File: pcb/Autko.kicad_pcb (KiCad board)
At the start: 2 copper layers, 140 x 155 mm, 124 parts, among them J1 PDI, M1 LEFT, M2 RIGHT, Q1 Si4368DY, Q2 BC817, SW1 POWER, SW2 START, SW3 STOP, U1 LTC3872, U10 CNY70, U11 TB6612FNG, U12 74HC14, U13 RN4678, U2 TLV1117-33, U3 ATxmega16A4U-A, U4 CNY70, U5 CNY70, U6 CNY70, U7 CNY70, U8 CNY70, U9 CNY70, Y1 8MHz

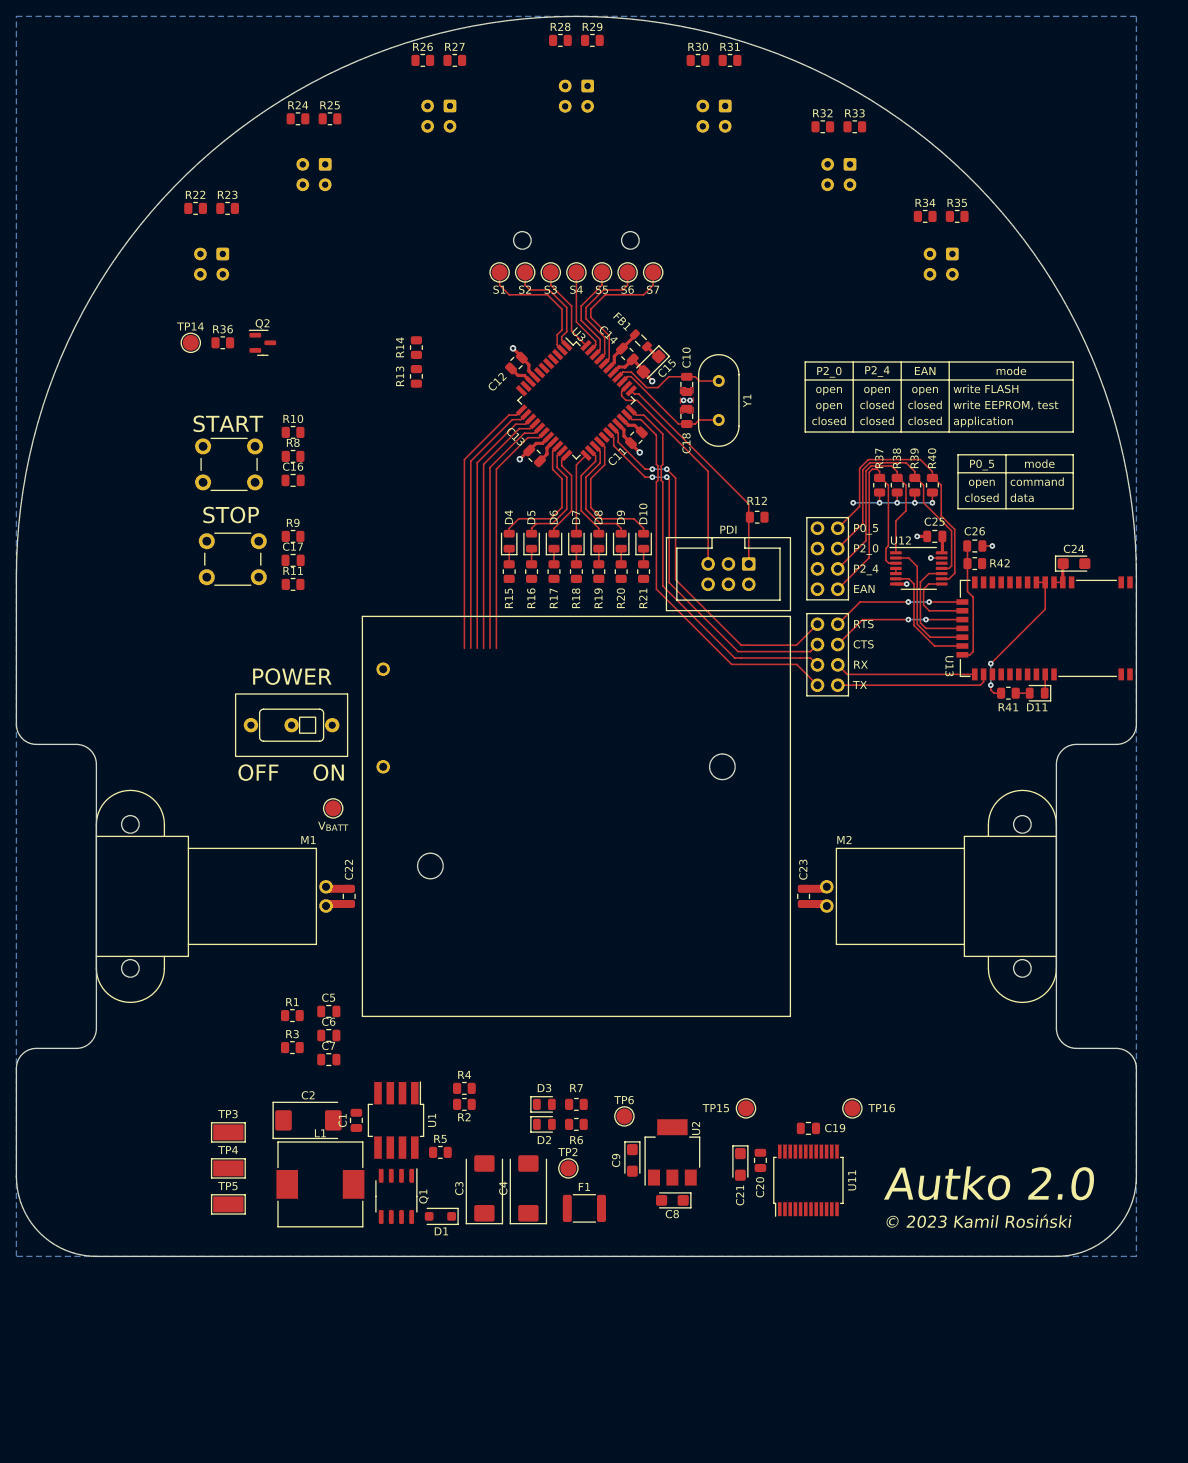
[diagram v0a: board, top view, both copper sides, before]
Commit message: [pcb] Line sensors routed
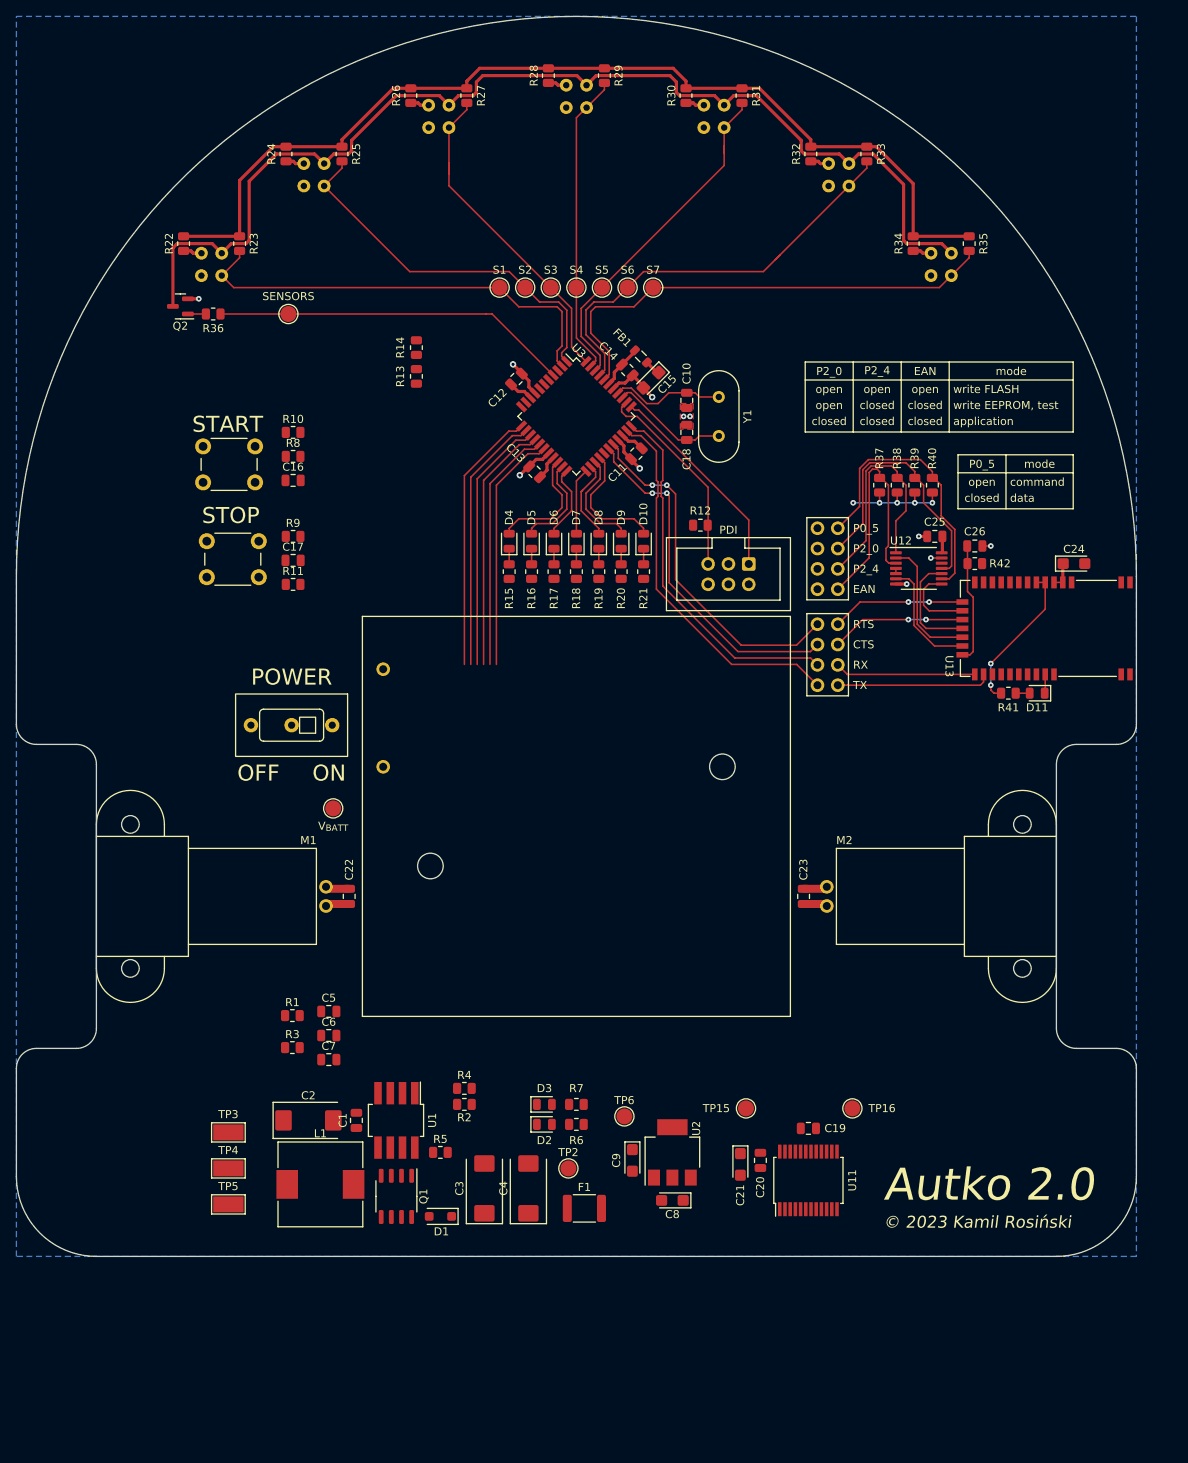
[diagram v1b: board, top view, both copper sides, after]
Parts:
- removed REF**: Pololu_ball_caster, Autko:Pololu_ball_caster
- U10, U4, U5, U6, U7, U8, U9: footprint OptoDevice:Vishay_CNY70 -> Autko:Vishay_CNY70
- moved TP14 12.7 mm to (63.5, 67.7)
- moved Q2 11.3 mm to (50.0, 66.8), turned to 180 degrees
- moved R12 7.17 mm to (115.0, 94.1), turned to 0 degrees
- moved R24 4.65 mm to (63.2, 47.7), turned to -90 degrees
- moved R25 4.65 mm to (70.2, 47.7), turned to -90 degrees
- moved R22 4.65 mm to (50.4, 58.9), turned to -90 degrees
- moved R23 4.65 mm to (57.4, 58.9), turned to -90 degrees
- moved R26 4.65 mm to (78.8, 40.4), turned to -90 degrees
- moved R27 4.65 mm to (85.8, 40.4), turned to -90 degrees
- moved R28 4.65 mm to (96.0, 37.9), turned to -90 degrees
- moved R29 4.65 mm to (103.0, 37.9), turned to -90 degrees
- moved R30 4.65 mm to (113.2, 40.4), turned to -90 degrees
- moved R31 4.65 mm to (120.2, 40.4), turned to -90 degrees
- moved R36 3.79 mm to (54.1, 67.7), turned to 180 degrees
- moved R32 3.72 mm to (128.8, 47.7), turned to -90 degrees
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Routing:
- net Net-(Q2-C): track 0.00 -> 140.2 mm
- net +3.3V: track 32.0 -> 157.6 mm
- net /Line sensors/IR_LEDS_ON: track 0.00 -> 44.8 mm
- net /Line sensors/SENSOR7: track 18.7 -> 60.7 mm
- net /Line sensors/SENSOR1: track 16.3 -> 55.7 mm
- net /Line sensors/SENSOR6: track 15.6 -> 53.5 mm
- net /Line sensors/SENSOR2: track 13.2 -> 47.7 mm
- net /Line sensors/SENSOR5: track 12.6 -> 44.0 mm
- net /Line sensors/SENSOR3: track 11.0 -> 41.7 mm
- net /Line sensors/SENSOR4: track 11.2 -> 38.3 mm
- net Net-(U10-A): track 0.00 -> 2.35 mm
- net Net-(U6-A): track 0.00 -> 2.35 mm
- net Net-(U4-A): track 0.00 -> 2.35 mm
- net Net-(U8-A): track 0.00 -> 2.35 mm
- net Net-(U7-A): track 0.00 -> 2.35 mm
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
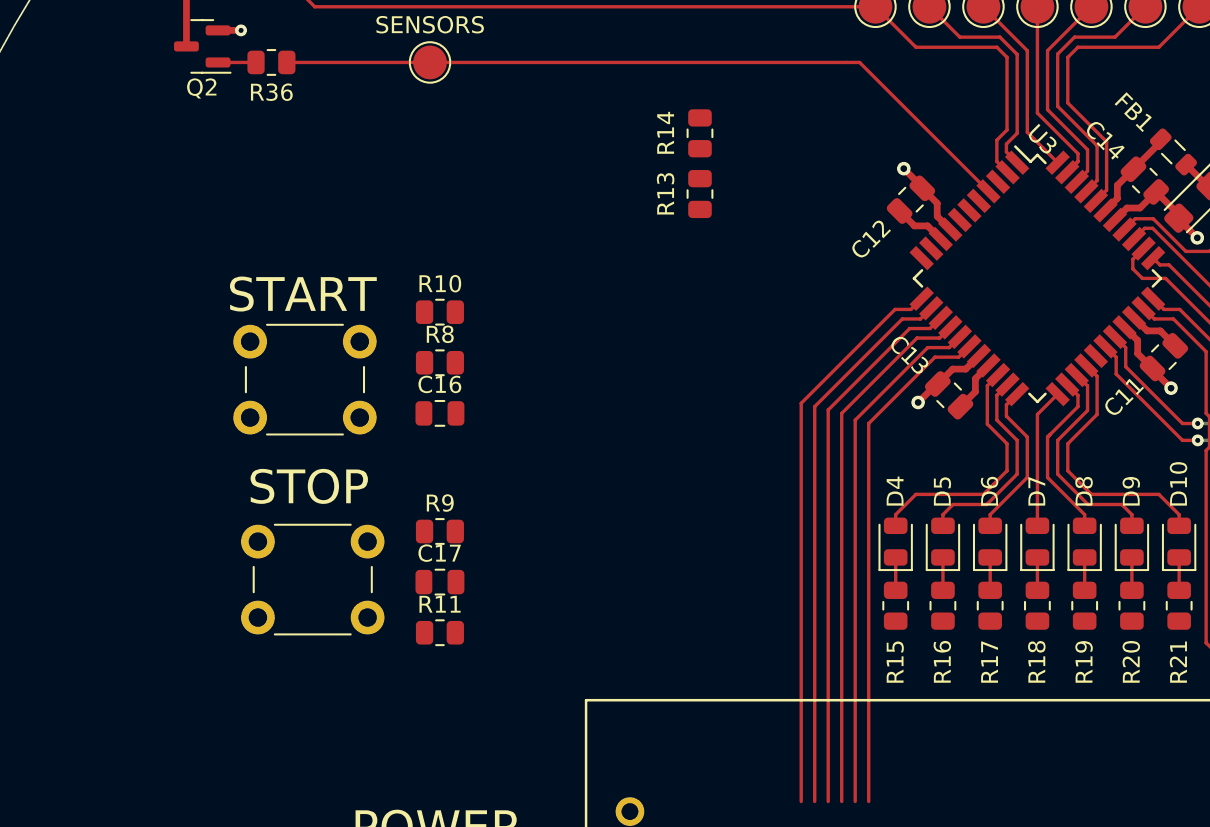
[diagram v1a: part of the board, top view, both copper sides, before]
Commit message: [pcb] Buttons routed
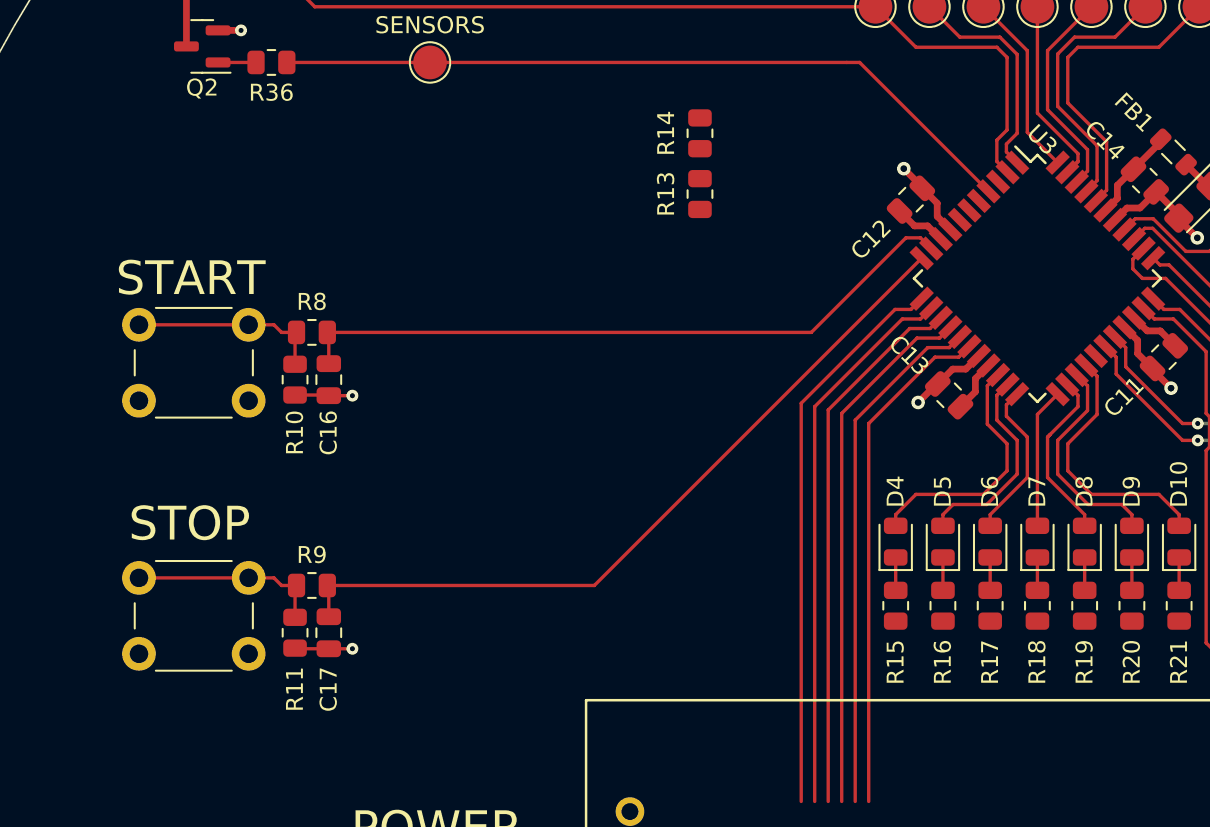
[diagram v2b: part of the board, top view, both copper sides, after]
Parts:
- moved R10 9.47 mm to (55.5, 86.5), turned to -90 degrees
- moved R11 8.59 mm to (55.5, 101.5), turned to -90 degrees
- moved R9 8.23 mm to (56.5, 98.7), turned to 180 degrees
- moved R8 7.80 mm to (56.5, 83.7), turned to 180 degrees
- moved SW3 7.37 mm to (46.2, 98.2)
- moved C17 7.24 mm to (57.5, 101.5), turned to -90 degrees
- moved C16 6.88 mm to (57.5, 86.5), turned to -90 degrees
- moved SW2 6.66 mm to (46.2, 83.2)
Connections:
- U3 pad 10: unconnected-(U3-PC0-Pad10) -> /Microcontroller/BTN_START
- U3 pad 11: unconnected-(U3-PC1-Pad11) -> /Microcontroller/BTN_STOP
- U3 pad 6: /Microcontroller/BTN_START -> unconnected-(U3-PB2-Pad6)
- U3 pad 7: /Microcontroller/BTN_STOP -> unconnected-(U3-PB3-Pad7)
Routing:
- net /Microcontroller/BTN_STOP: track 0.00 -> 45.2 mm
- net /Microcontroller/BTN_START: track 0.00 -> 40.3 mm
- net Net-(R11-Pad1): track 0.00 -> 11.4 mm
- net Net-(R10-Pad1): track 0.00 -> 11.4 mm
- net GND: track 27.3 -> 34.1 mm, vias 11 -> 13
